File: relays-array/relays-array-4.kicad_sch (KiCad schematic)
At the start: 39 parts, among them J1 NMJ6HCD2, J10 Screw_Terminal_01x02, J14 NMJ6HCD2, J15 Screw_Terminal_01x02, J2 NMJ6HCD2, J3 Screw_Terminal_01x02, J4 NMJ6HCD2, J5 NMJ6HCD2, J6 Screw_Terminal_01x02, K1 G2RL-2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

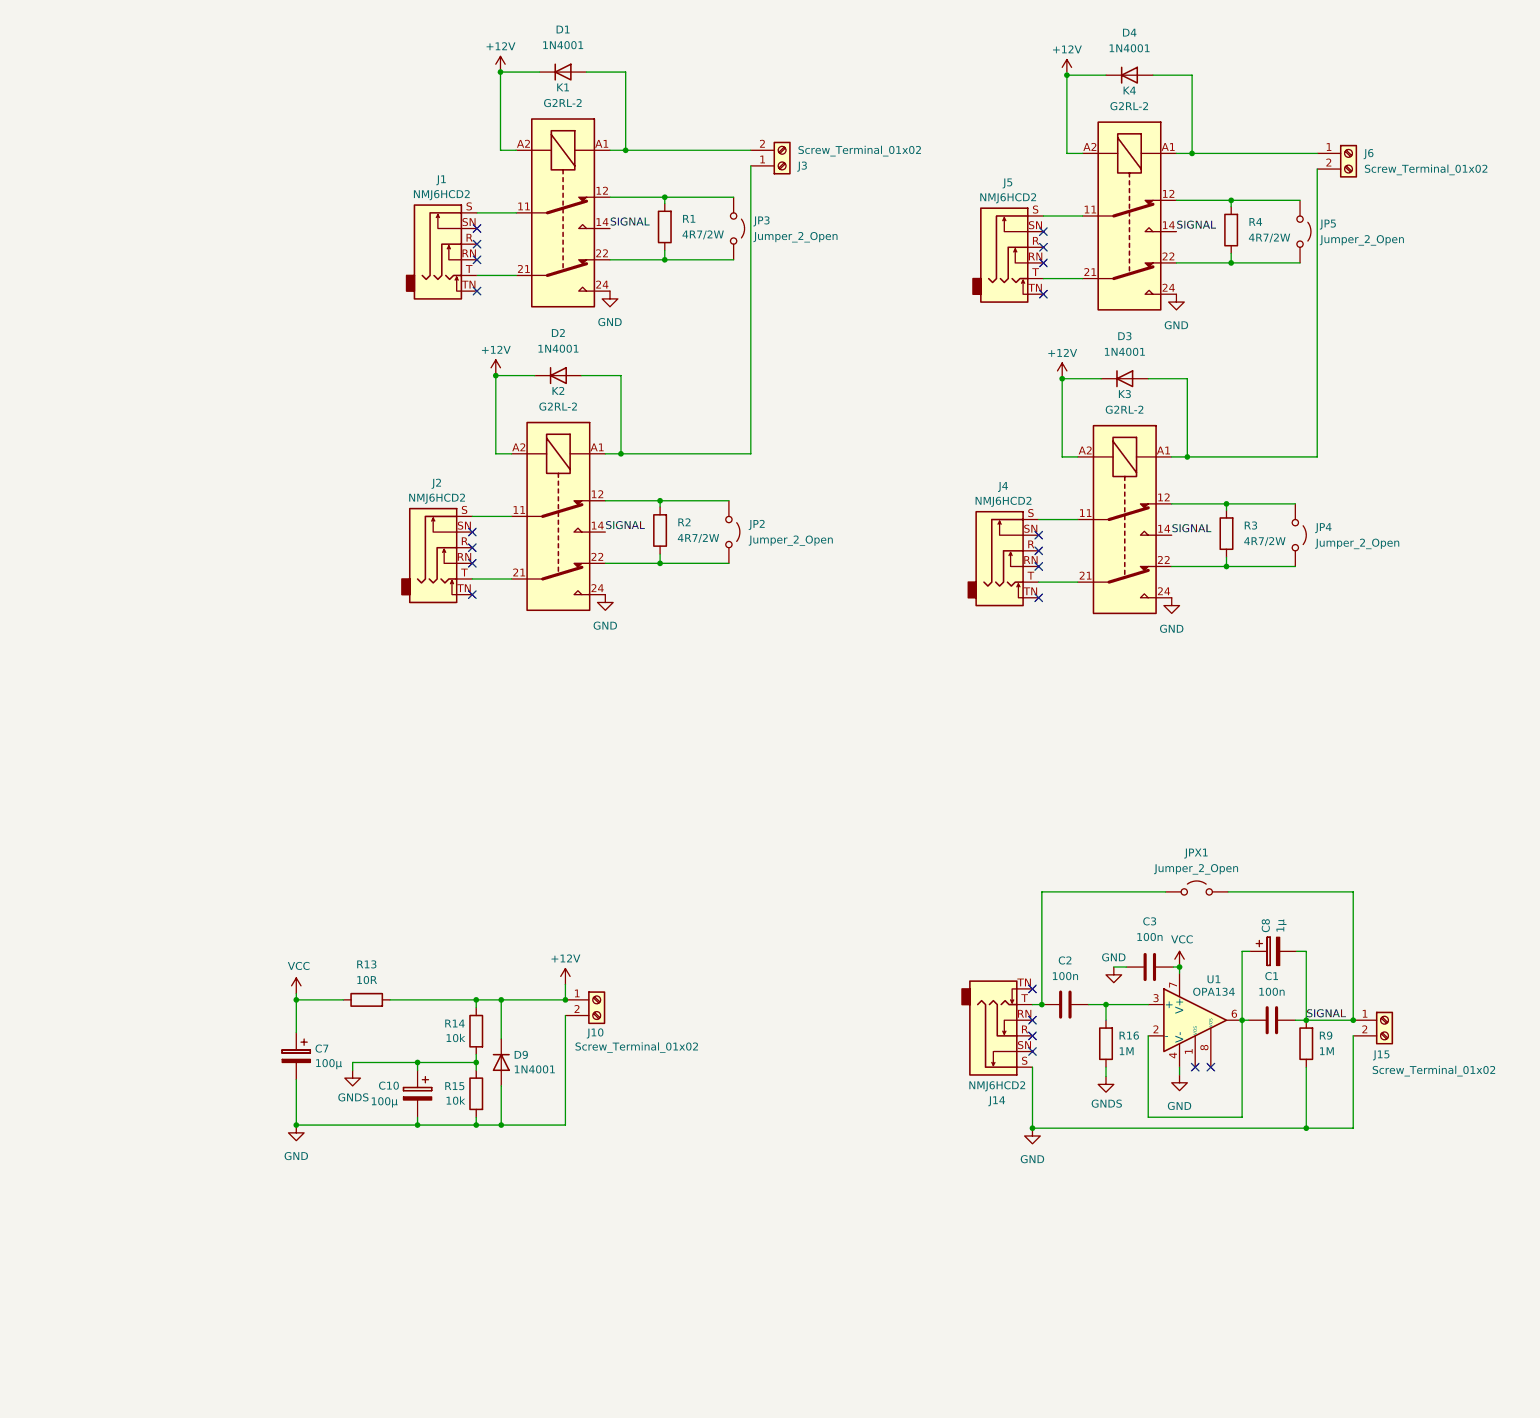
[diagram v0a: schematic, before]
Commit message: relays-array: add terminal block for buffer use w/ external connector
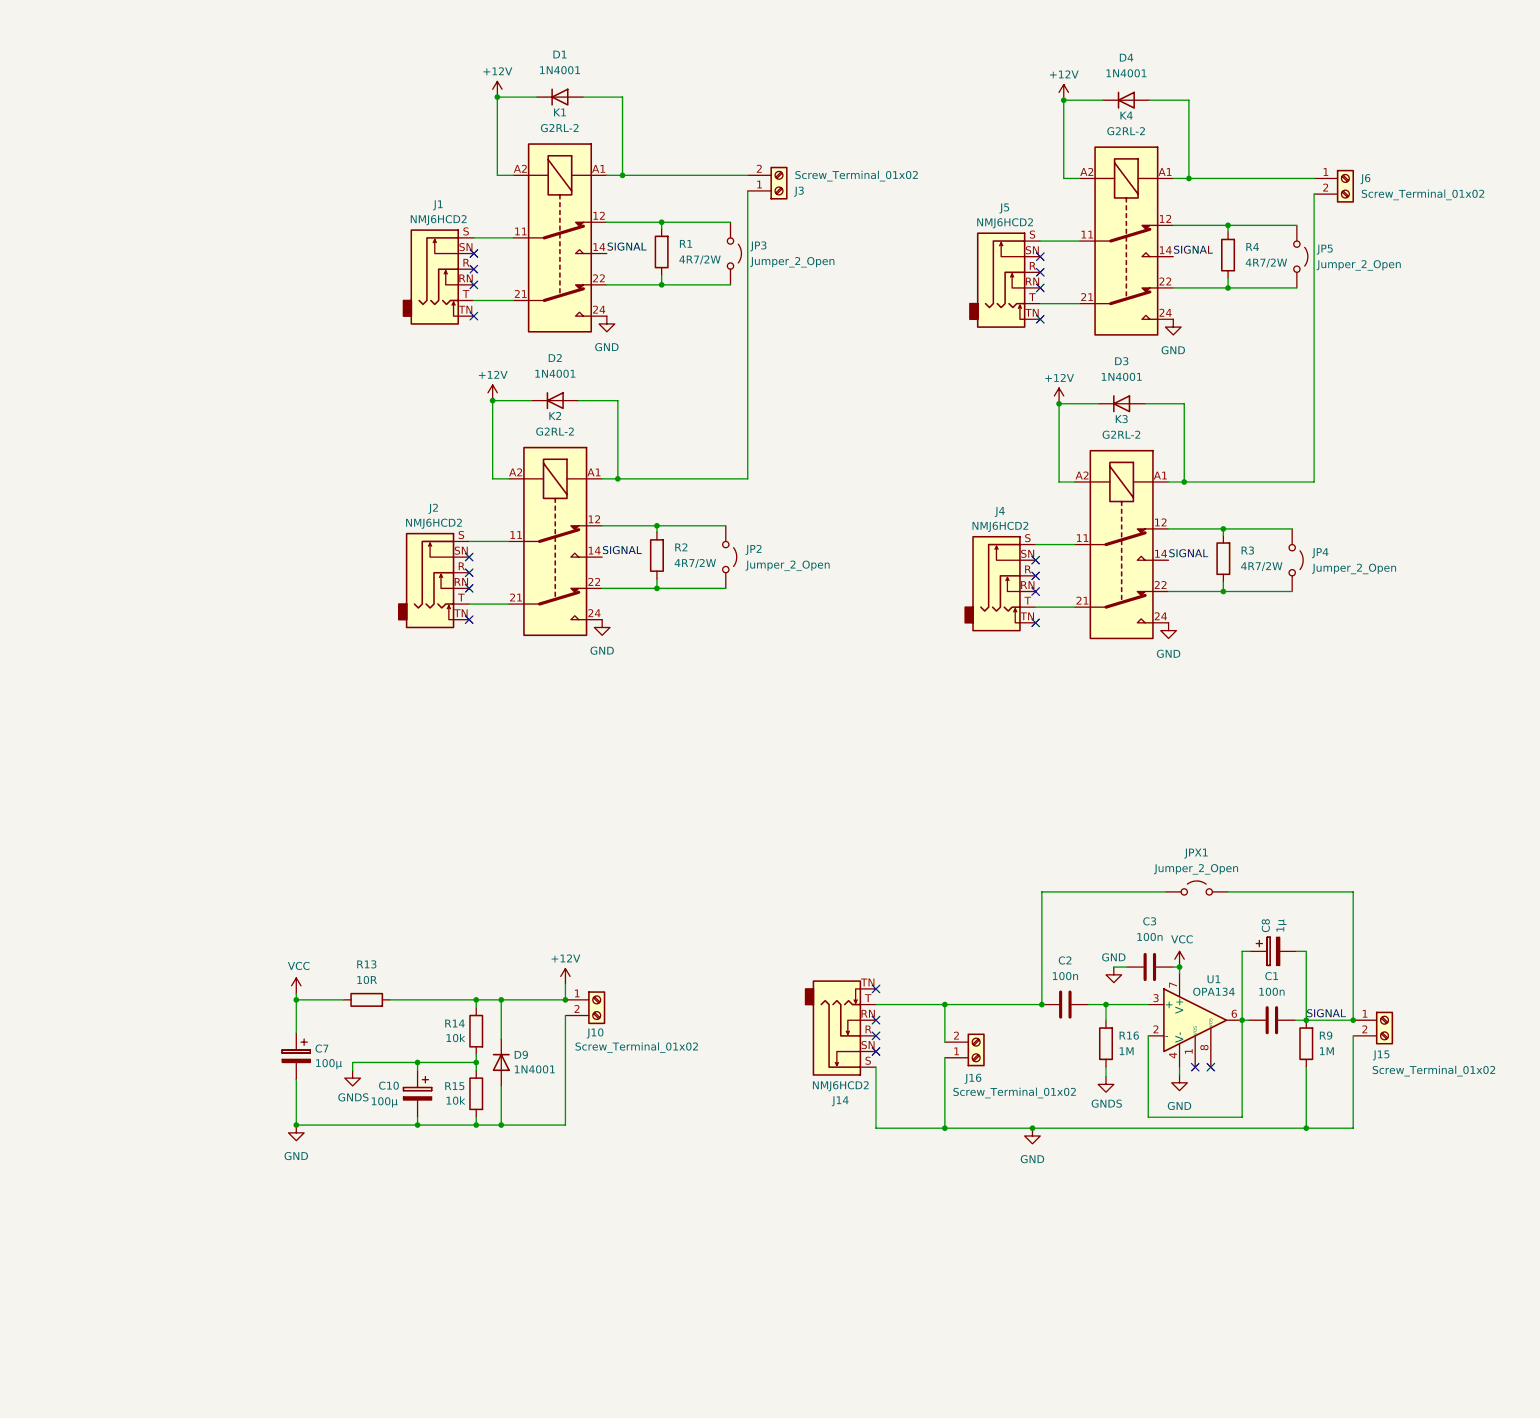
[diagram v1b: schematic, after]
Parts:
- added J16: Screw_Terminal_01x02, TerminalBlock:TerminalBlock_bornier-2_P5.08mm, symbol Connector:Screw_Terminal_01x02
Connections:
- net GND: now also J16.1 (Pin_1)
- net at C2.2, J14.T, JPX1.2 (B): now also J16.2 (Pin_2)
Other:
- moved on the sheet: D1, D2, D3, D4, J1, J14, J2, J3, J4, J5, J6, JP2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

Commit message: relays-array: fix schematics error and add ground plane
The jack connectors are all (except for the buffer input) wired
backwards, with the tip going to `GND` and the sleeve on `SIGNAL`, while
it should be the other way around.

While at it, improve a bit the PCB tracks and add a ground plane. The
latter is only connected to `GND` in a single point in order to avoid
ground loops and other unpleasant issues.
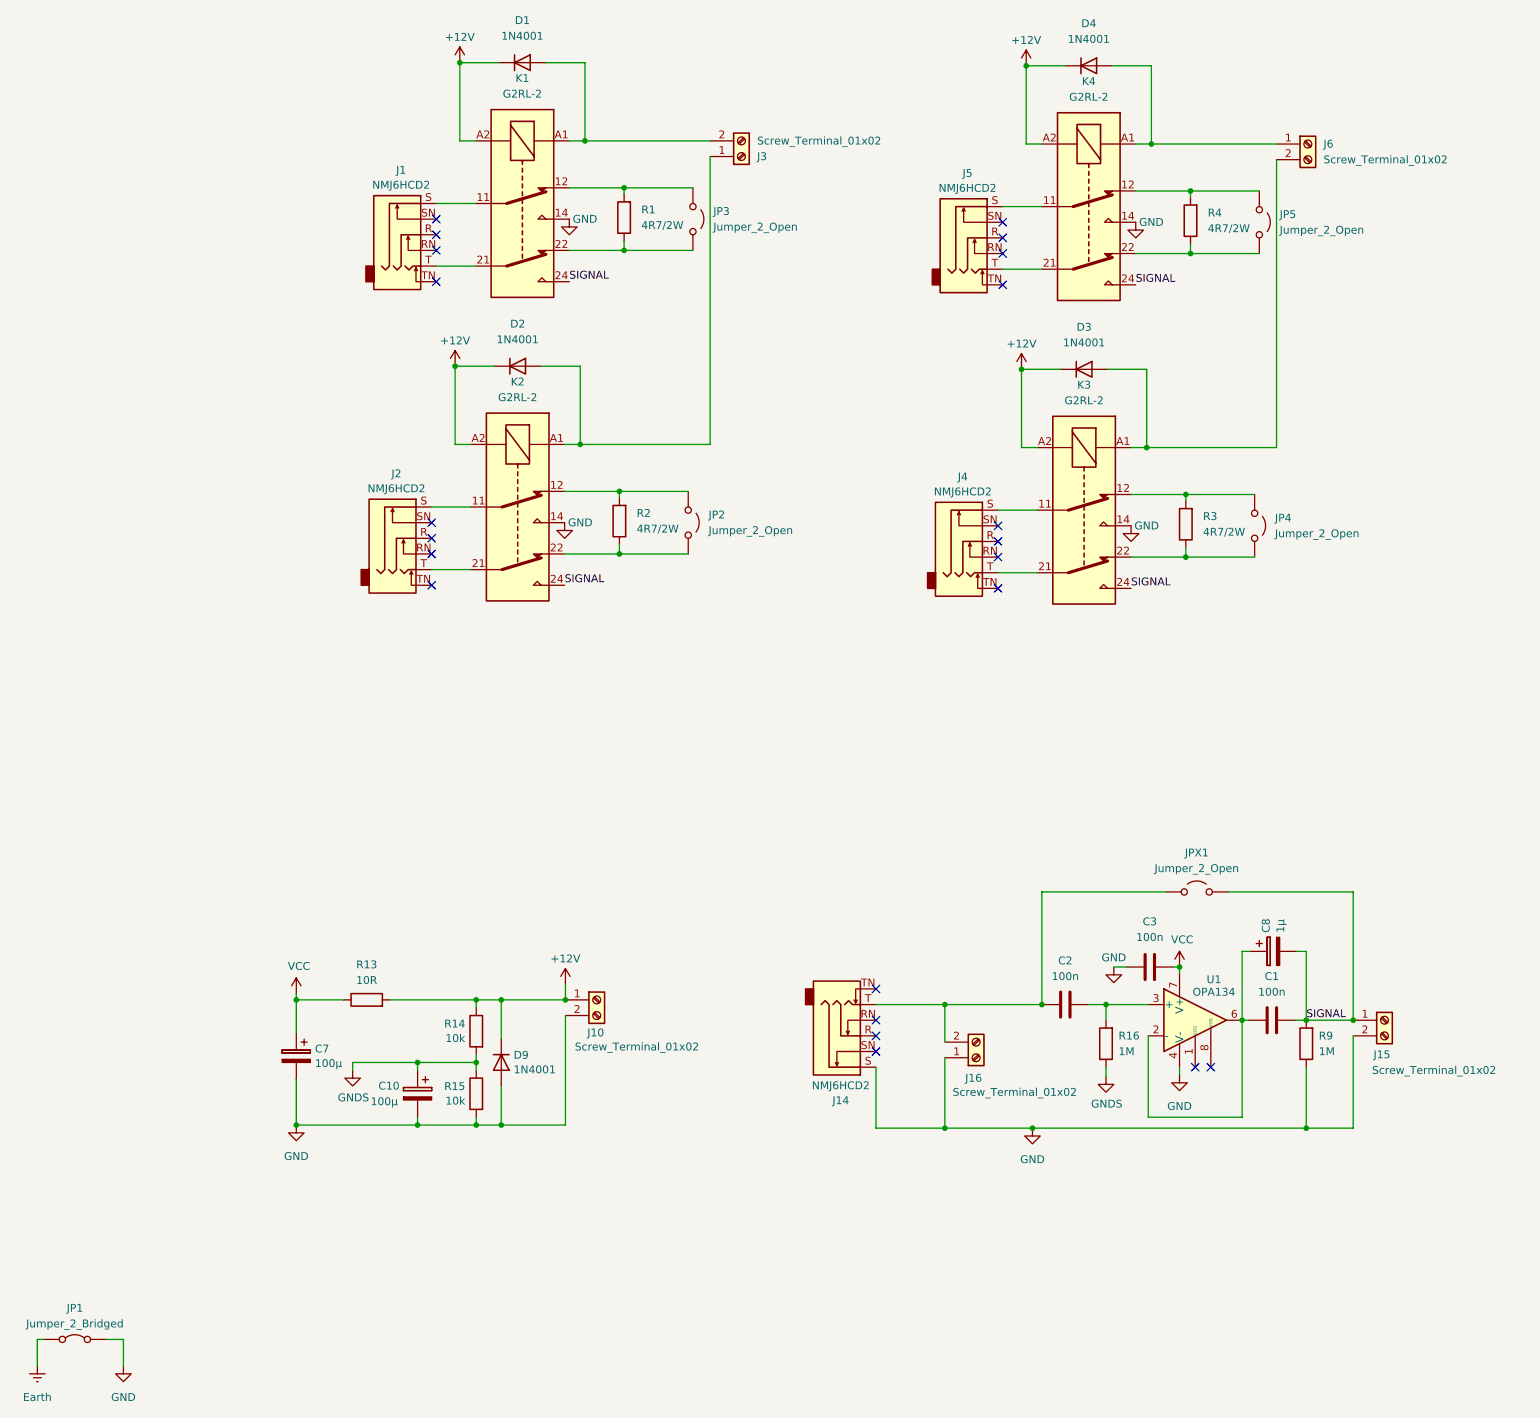
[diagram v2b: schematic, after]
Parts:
- added JP1: Jumper_2_Bridged, Jumper:SolderJumper-2_P1.3mm_Bridged_RoundedPad1.0x1.5mm, symbol Jumper:Jumper_2_Bridged
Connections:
- net GND: now also K1.14, K2.14, K3.14, K4.14, JP1.2 (B); no longer K1.24, K2.24, K3.24, K4.24
- net SIGNAL: now also K1.24, K2.24, K3.24, K4.24; no longer K1.14, K2.14, K3.14, K4.14
- new net Earth: JP1.1 (A)
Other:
- moved on the sheet: D1, D2, D3, D4, J1, J2, J3, J4, J5, J6, JP2, JP3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
